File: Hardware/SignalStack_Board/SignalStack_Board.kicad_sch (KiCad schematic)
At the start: 63 parts, among them J1 Molex_uF_SV_06, J2 RJ45_LED_Shielded, Q1 SI4156DY, Q2 SI4156DY, Q3 SI4156DY, Q4 SI4156DY, Q5 SI4156DY, Q6 SI4156DY, Q7 SI4156DY, Q8 SI4156DY, U1 OKI, U2 Teensy4.1_DEV-16771, U3 IRS2005S, U4 IRS2005S, U5 IRS2005S, U6 IRS2005S, U7 MMC5633NJL, U8 SMAJ12CA

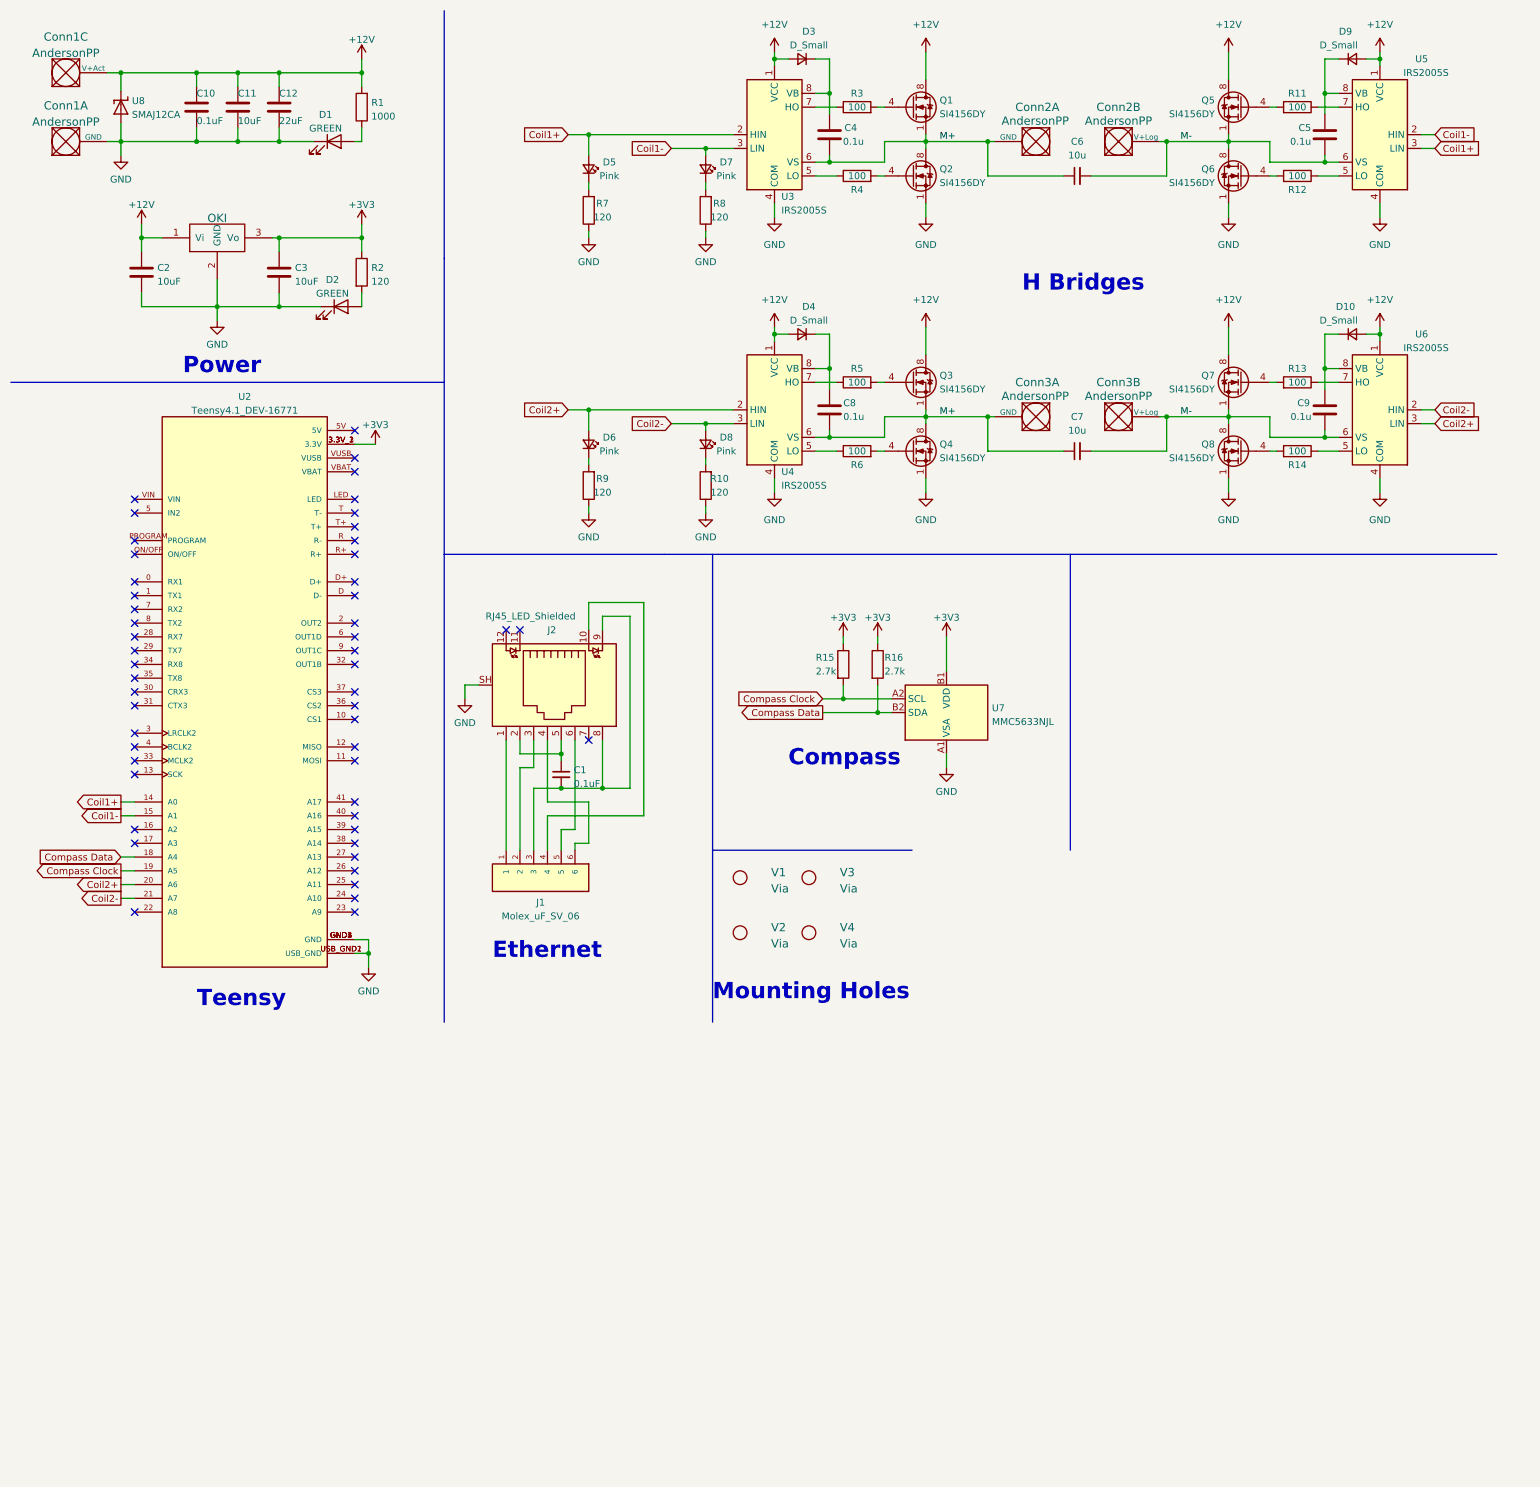
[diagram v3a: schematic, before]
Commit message: Started GPS connector
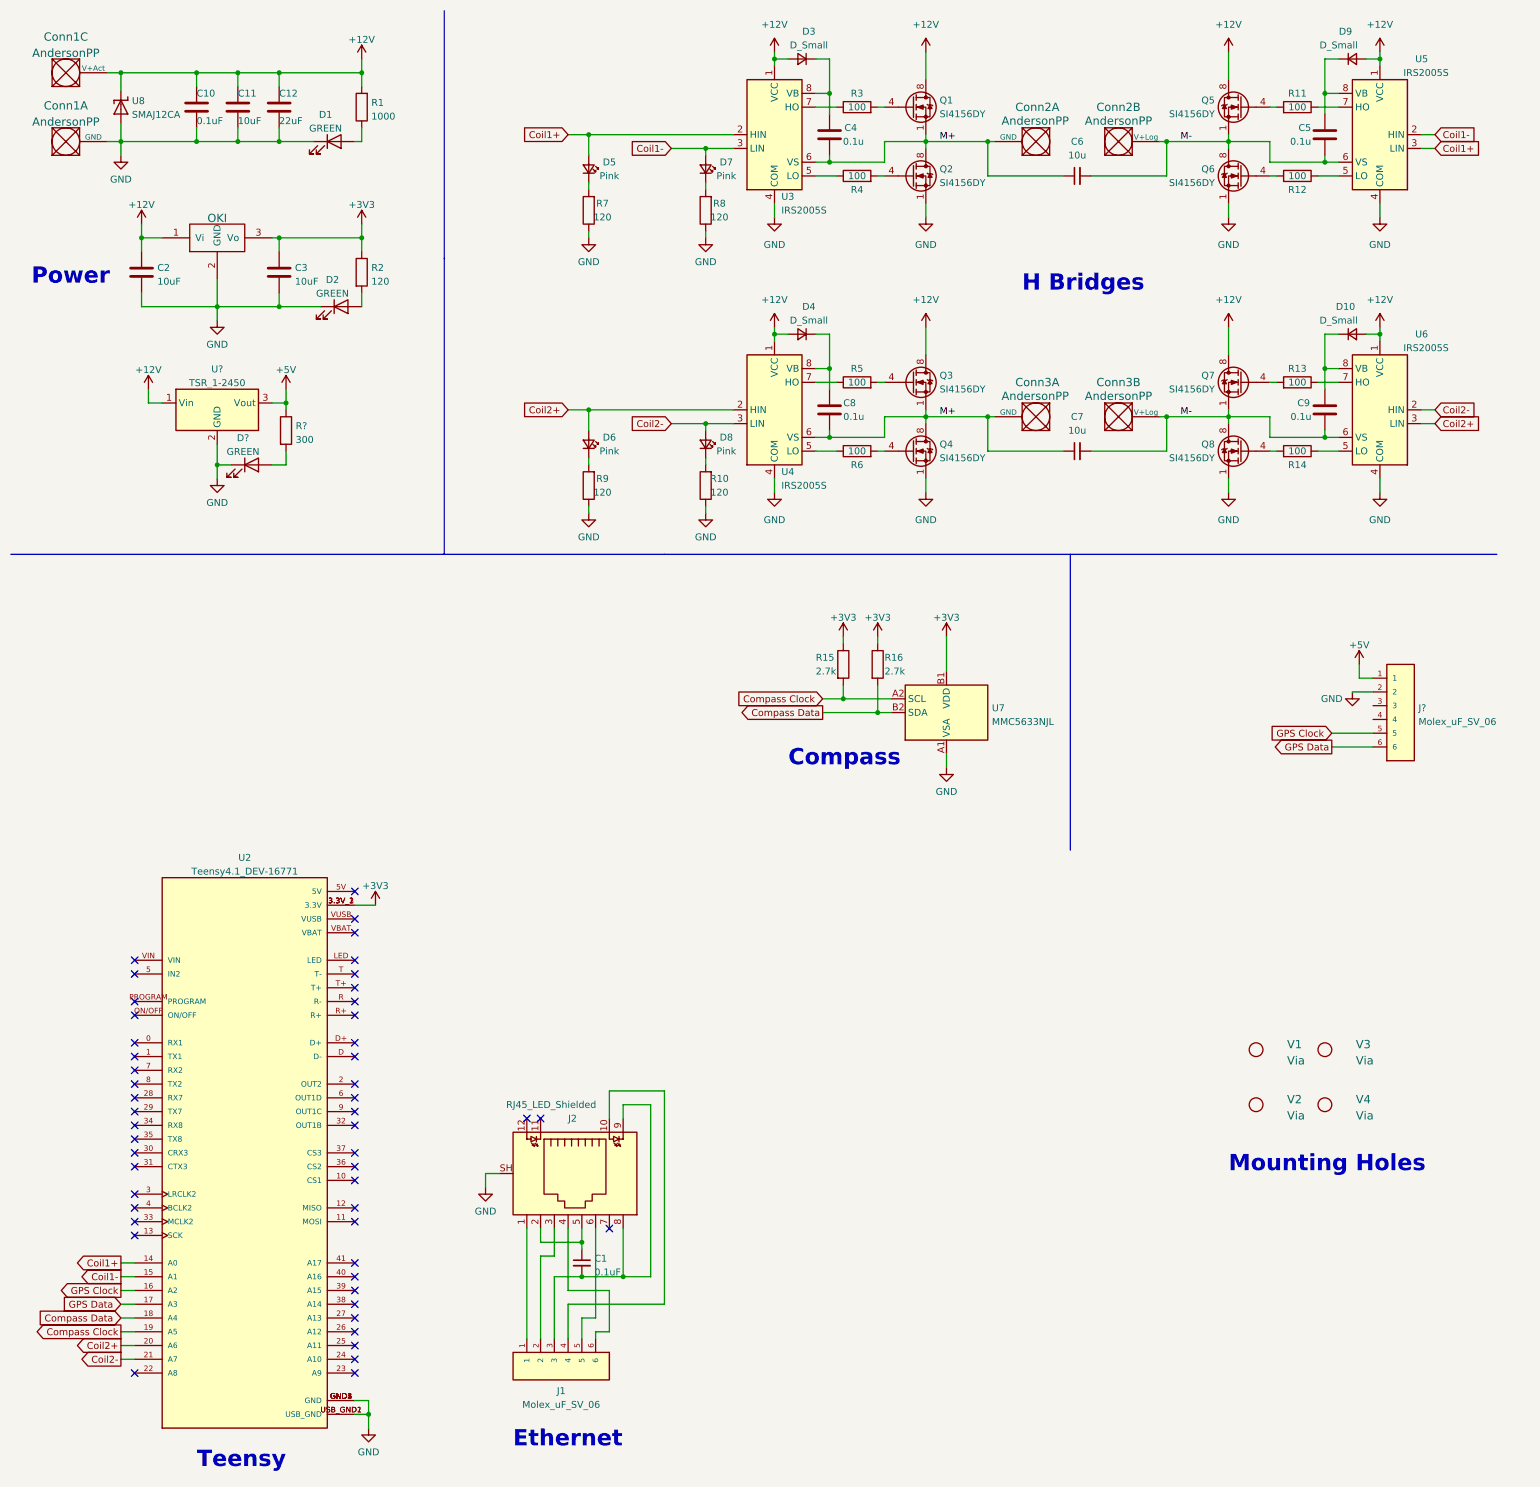
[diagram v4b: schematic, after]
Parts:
- added D?: GREEN, symbol Device:LED
- added J?: Molex_uF_SV_06, MRDT_Connectors:MOLEX_uF_S_06_Vertical, symbol MRDT_Connectors:Molex_uF_SV_06
- added R?: 300, symbol Device:R
- added U?: TSR_1-2450, Converter_DCDC:Converter_DCDC_TRACO_TSR-1_THT, symbol Regulator_Switching:TSR_1-2450
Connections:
- net +12V: now also U?.1 (Vin)
- net GND: now also D?.1 (K), J?.2, U?.2 (GND)
- net GPS Clock: now reaches U2.16 (A2)
- net GPS Clock: now also J?.5
- net GPS Data: now reaches U2.17 (A3)
- net GPS Data: now also J?.6
- new net: D?.2 (A), R?.2
- new net +5V: J?.1, R?.1, U?.3 (Vout)
- no-connect marks 52 -> 50
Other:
- moved on the sheet: C1, J1, J2, U2, V1, V2, V3, V4

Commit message: Rearranged schematic
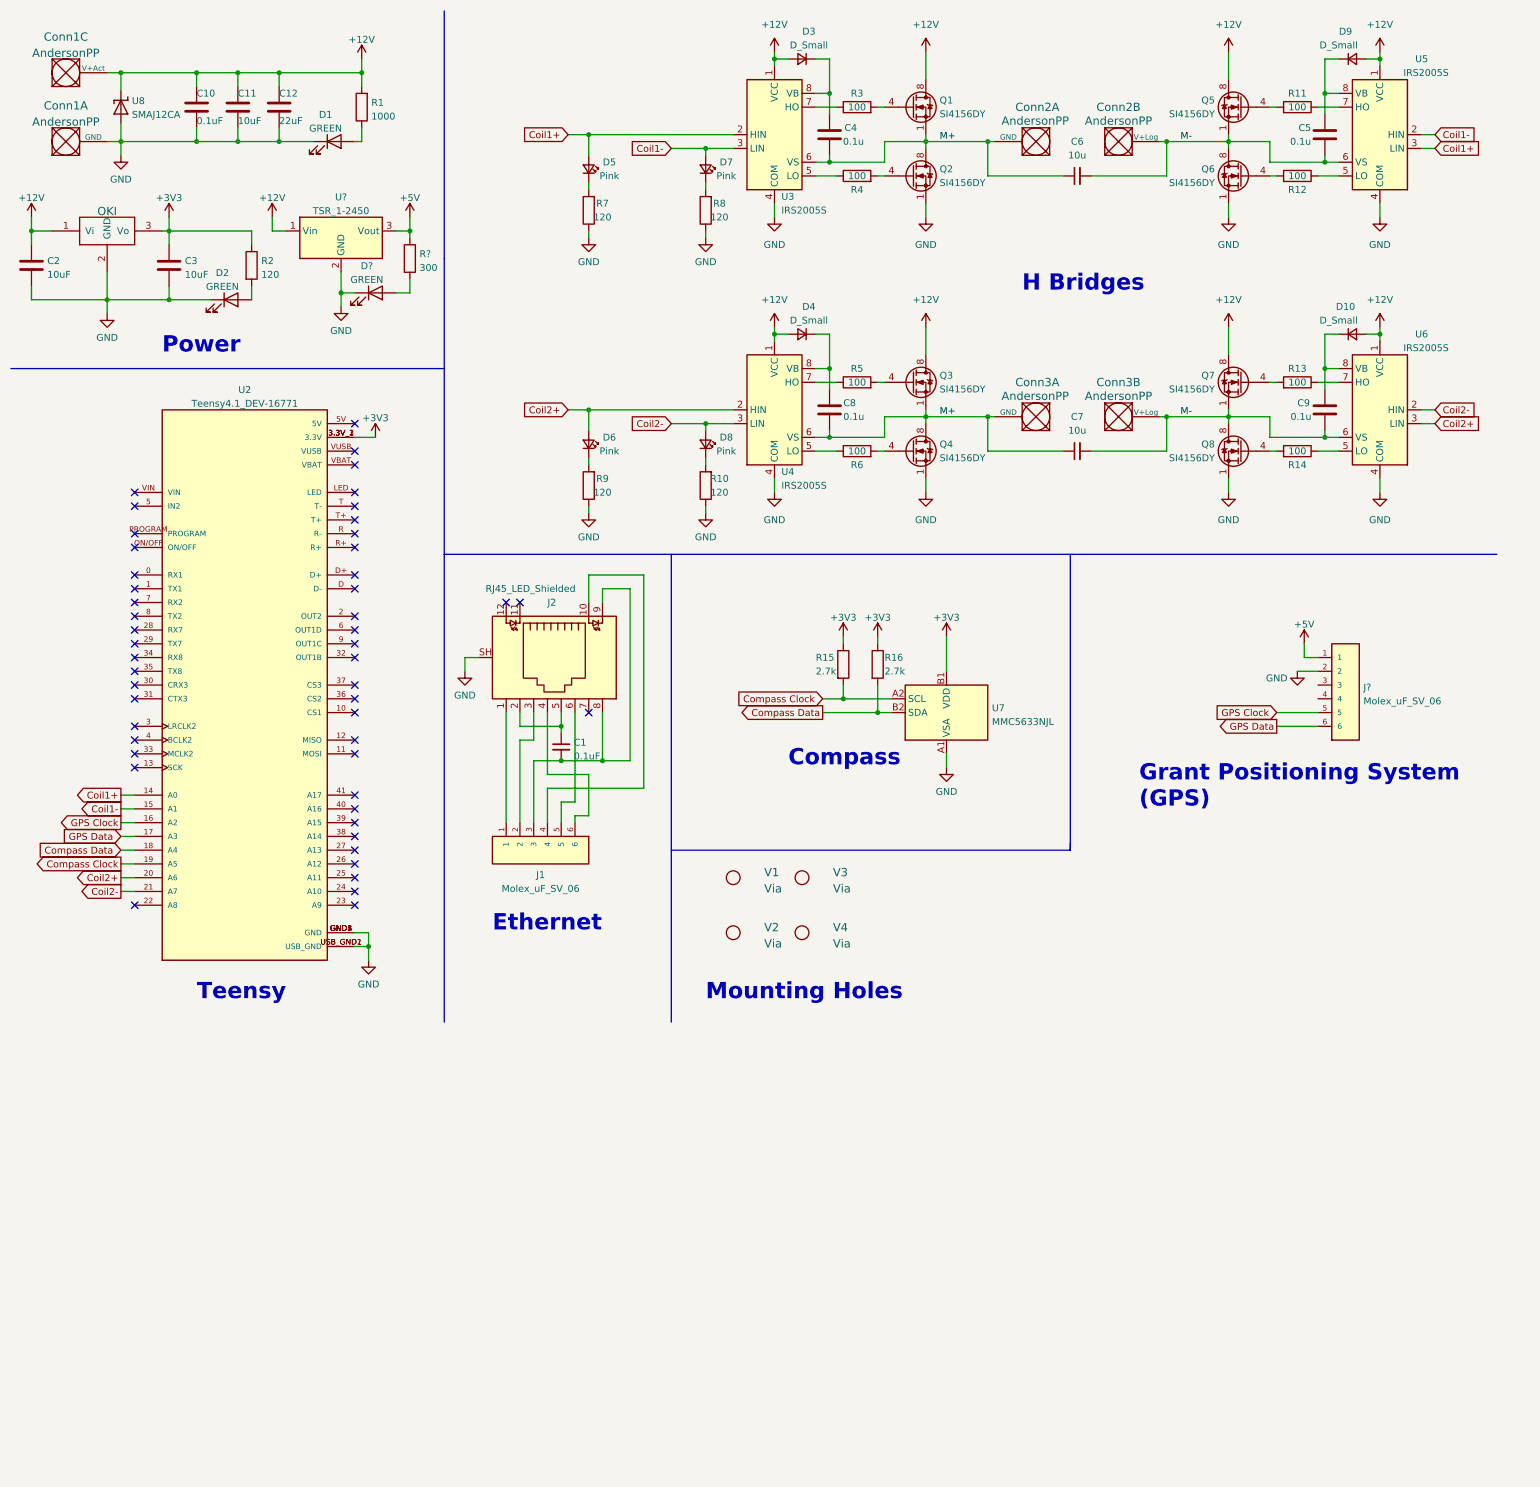
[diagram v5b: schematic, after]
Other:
- note added: "Grant Positioning System (GPS)"
- moved on the sheet: C1, C2, C3, D2, D?, J1, J2, J?, R2, R?, U2, U?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
